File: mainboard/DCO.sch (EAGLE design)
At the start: 44 parts, among them IC101 LF353D, IC201 LF353D, IC3 V_REG_MIC2920, J3 M04X2, P101 TRIMPOT 100K

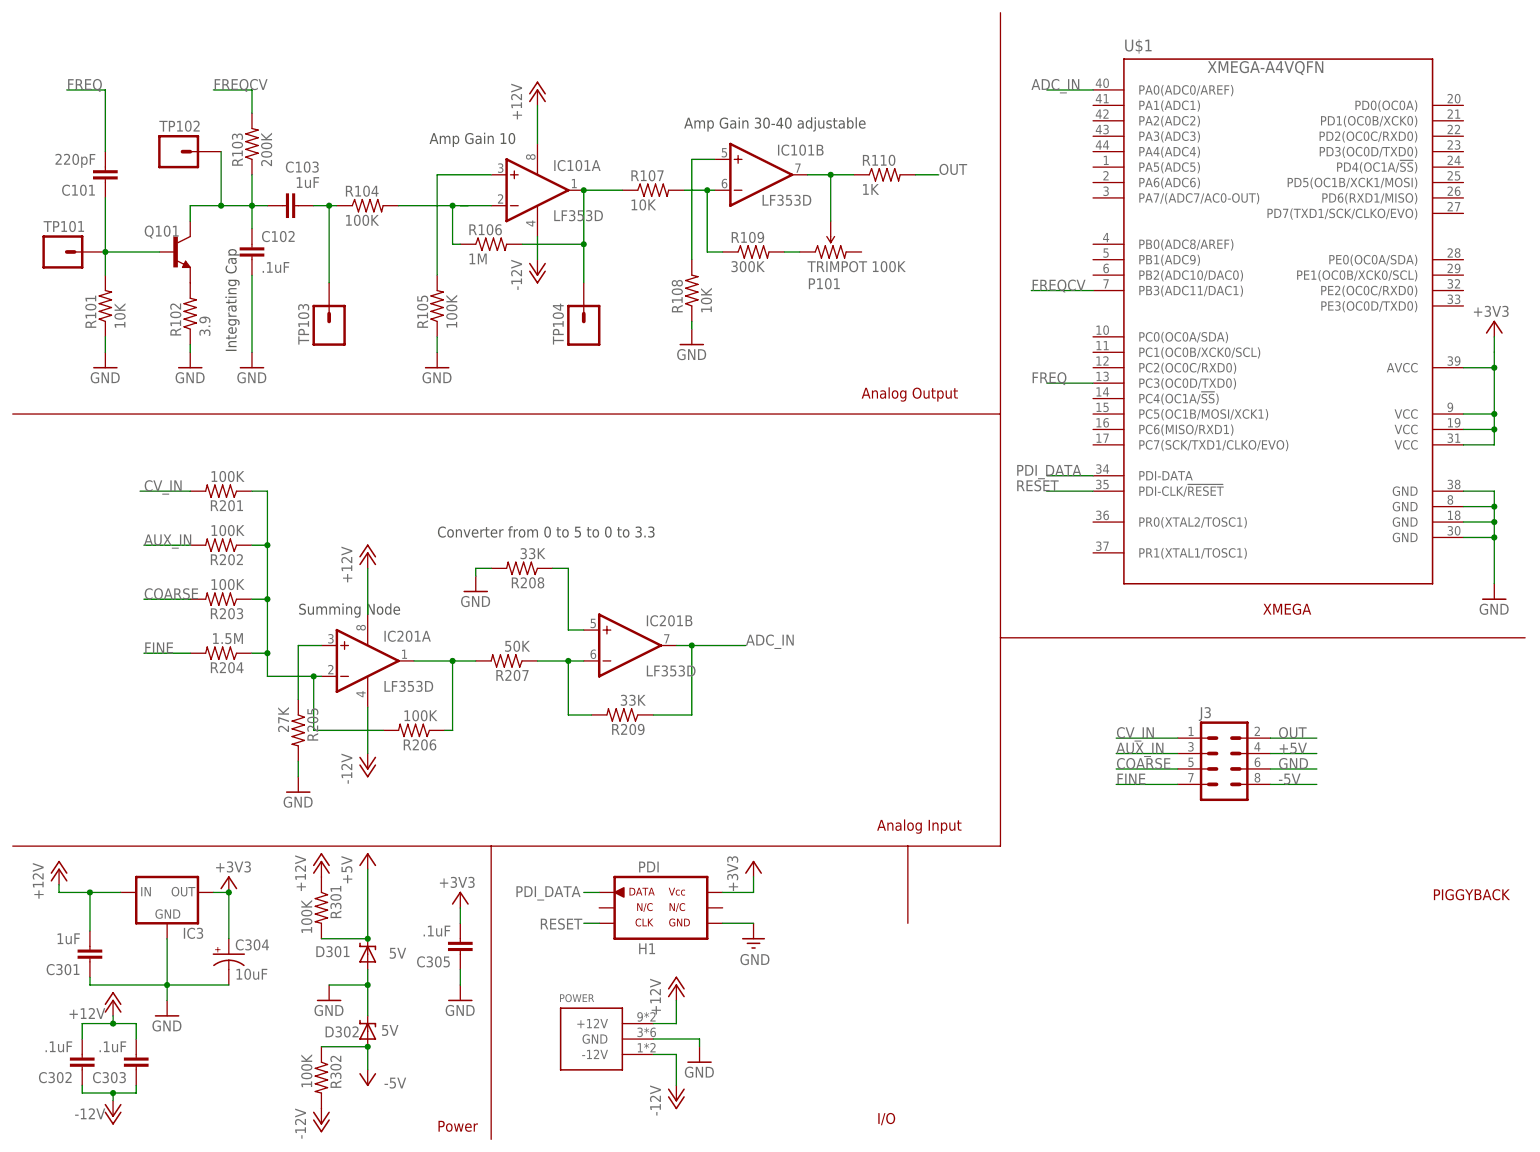
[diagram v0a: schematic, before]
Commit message: Re-laid out board, no routing
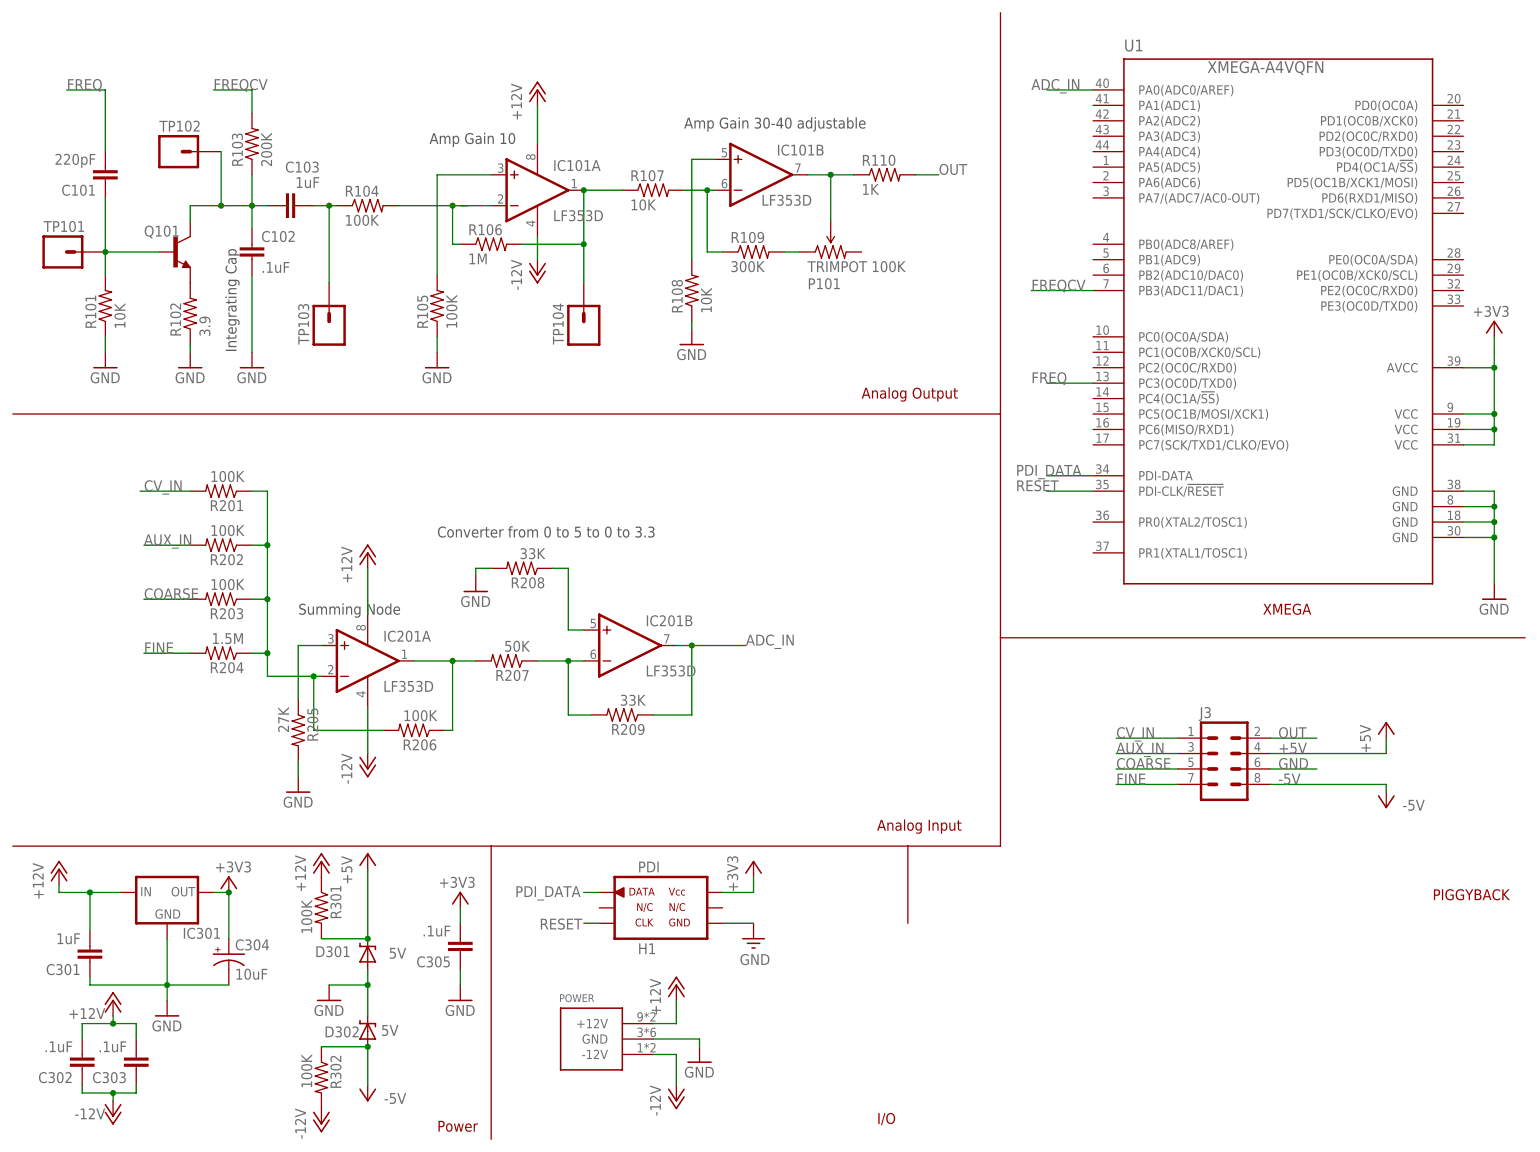
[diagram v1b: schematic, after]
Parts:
- renumbered IC3 to IC301, U$1 to U1
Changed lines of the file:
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@@
 <setting verticaltext="up"/>
 </settings>
-<grid distance="0.05" unitdist="inch" unit="inch" style="lines" multiple="1" display="no" altdistance="0.01" altunitdist="inch" altunit="inch"/>
+<grid distance="0.05" unitdist="inch" unit="inch" style="lines" multiple="1" display="yes" altdistance="0.01" altunitdist="inch" altunit="inch"/>
 <layers>
 <layer number="1" name="Top" color="4" fill="1" visible="no" active="no"/>
@@
 <part name="R207" library="SparkFun" deviceset="RESISTOR" device="0603-RES" value="50K"/>
 <part name="R209" library="SparkFun" deviceset="RESISTOR" device="0603-RES" value="33K"/>
-<part name="IC3" library="SparkFun" deviceset="V_REG_MIC2920" device="" value=""/>
+<part name="IC301" library="SparkFun" deviceset="V_REG_MIC2920" device="" value=""/>
 <part name="C301" library="SparkFun" deviceset="CAP" device="0603-CAP" value="1uF"/>
 <part name="C304" library="SparkFun" deviceset="CAP_POL" device="1206" value="10uF"/>
@@
 <part name="P+6" library="supply1" deviceset="+5V" device=""/>
 <part name="GND12" library="SparkFun" deviceset="GND" device=""/>
-<part name="U$1" library="custom" deviceset="XMEGA-A4" device="VQFN"/>
+<part name="U1" library="custom" deviceset="XMEGA-A4" device="VQFN"/>
 <part name="+3V2" library="supply1" deviceset="+3V3" device=""/>
 <part name="GND11" library="supply1" deviceset="GND" device=""/>
@@
 <part name="+3V4" library="supply1" deviceset="+3V3" device=""/>
 <part name="P+1" library="supply1" deviceset="+12V" device=""/>
+<part name="P+2" library="supply1" deviceset="+5V" device=""/>
+<part name="P-1" library="supply1" deviceset="-5V" device=""/>
 </parts>
 <sheets>
@@
 <instance part="R207" gate="G$1" x="81.28" y="78.74" rot="R180"/>
 <instance part="R209" gate="G$1" x="100.33" y="69.85" rot="R180"/>
-<instance part="IC3" gate="G$1" x="25.4" y="40.64"/>
+<instance part="IC301" gate="G$1" x="25.4" y="40.64"/>
 <instance part="C301" gate="G$1" x="12.7" y="31.75" rot="R180"/>
 <instance part="C304" gate="G$1" x="35.56" y="30.48"/>
@@
 <instance part="P+5" gate="1" x="50.8" y="45.72"/>
 <instance part="P-4" gate="1" x="50.8" y="2.54"/>
-<instance part="P-5" gate="1" x="58.42" y="8.89" smashed="yes">
-<attribute name="VALUE" x="64.77" y="10.16" size="1.778" layer="96" rot="R180"/>
+<instance part="P-5" gate="1" x="58.42" y="6.35" smashed="yes">
+<attribute name="VALUE" x="64.77" y="7.62" size="1.778" layer="96" rot="R180"/>
 </instance>
 <instance part="P+6" gate="1" x="58.42" y="46.99"/>
 <instance part="GND12" gate="1" x="243.84" y="88.9"/>
-<instance part="U$1" gate="G$1" x="208.28" y="137.16"/>
+<instance part="U1" gate="G$1" x="208.28" y="137.16"/>
 <instance part="+3V2" gate="G$1" x="73.66" y="40.64" smashed="yes">
 <attribute name="VALUE" x="76.2" y="43.18" size="1.778" layer="96" rot="R180"/>
@@
 </instance>
 <instance part="P+1" gate="1" x="86.36" y="172.72"/>
+<instance part="P+2" gate="1" x="226.06" y="68.58"/>
+<instance part="P-1" gate="1" x="226.06" y="54.61" smashed="yes">
+<attribute name="VALUE" x="232.41" y="55.88" size="1.778" layer="96" rot="R180"/>
+</instance>
 </instances>
 <busses>
@@
 </segment>
 <segment>
-<pinref part="U$1" gate="G$1" pin="PC3(OC0D/TXD0)"/>
+<pinref part="U1" gate="G$1" pin="PC3(OC0D/TXD0)"/>
 <wire x1="177.8" y1="124.46" x2="170.18" y2="124.46" width="0.1524" layer="91"/>
 <label x="167.64" y="124.46" size="1.778" layer="95"/>
@@
 </segment>
 <segment>
-<pinref part="U$1" gate="G$1" pin="PB3(ADC11/DAC1)"/>
+<pinref part="U1" gate="G$1" pin="PB3(ADC11/DAC1)"/>
 <wire x1="177.8" y1="139.7" x2="167.64" y2="139.7" width="0.1524" layer="91"/>
 <label x="167.64" y="139.7" size="1.778" layer="95"/>
@@
 </segment>
 <segment>
-<pinref part="IC3" gate="G$1" pin="GND"/>
+<pinref part="IC301" gate="G$1" pin="GND"/>
 <pinref part="GND9" gate="1" pin="GND"/>
 <wire x1="25.4" y1="33.02" x2="25.4" y2="25.4" width="0.1524" layer="91"/>
@@
 <junction x="243.84" y="99.06"/>
 <pinref part="GND12" gate="1" pin="GND"/>
-<pinref part="U$1" gate="G$1" pin="GND@1"/>
-<pinref part="U$1" gate="G$1" pin="GND@2"/>
-<pinref part="U$1" gate="G$1" pin="GND@3"/>
-<pinref part="U$1" gate="G$1" pin="GND@4"/>
+<pinref part="U1" gate="G$1" pin="GND@1"/>
+<pinref part="U1" gate="G$1" pin="GND@2"/>
+<pinref part="U1" gate="G$1" pin="GND@3"/>
+<pinref part="U1" gate="G$1" pin="GND@4"/>
 </segment>
 <segment>
@@
 <segment>
 <pinref part="J3" gate="G$1" pin="4"/>
-<wire x1="207.01" y1="63.5" x2="214.63" y2="63.5" width="0.1524" layer="91"/>
 <label x="208.28" y="63.5" size="1.778" layer="95"/>
+<wire x1="207.01" y1="63.5" x2="226.06" y2="63.5" width="0.1524" layer="91"/>
+<pinref part="P+2" gate="1" pin="+5V"/>
+<wire x1="226.06" y1="63.5" x2="226.06" y2="66.04" width="0.1524" layer="91"/>
 </segment>
 </net>
 <net name="-5V" class="0">
+<segment>
+<pinref part="J3" gate="G$1" pin="8"/>
+<label x="208.28" y="58.42" size="1.778" layer="95"/>
+<wire x1="207.01" y1="58.42" x2="226.06" y2="58.42" width="0.1524" layer="91"/>
+<pinref part="P-1" gate="1" pin="-5V"/>
+<wire x1="226.06" y1="58.42" x2="226.06" y2="57.15" width="0.1524" layer="91"/>
+</segment>
 <segment>
 <pinref part="D302" gate="G$1" pin="A"/>
@@
 <wire x1="58.42" y1="15.24" x2="50.8" y2="15.24" width="0.1524" layer="91"/>
 <pinref part="P-5" gate="1" pin="-5V"/>
-<wire x1="58.42" y1="15.24" x2="58.42" y2="11.43" width="0.1524" layer="91"/>
+<wire x1="58.42" y1="15.24" x2="58.42" y2="8.89" width="0.1524" layer="91"/>
 <junction x="58.42" y="15.24"/>
-</segment>
-<segment>
-<pinref part="J3" gate="G$1" pin="8"/>
-<wire x1="207.01" y1="58.42" x2="214.63" y2="58.42" width="0.1524" layer="91"/>
-<label x="208.28" y="58.42" size="1.778" layer="95"/>
 </segment>
 </net>
@@
 </segment>
 <segment>
-<pinref part="U$1" gate="G$1" pin="PA0(ADC0/AREF)"/>
+<pinref part="U1" gate="G$1" pin="PA0(ADC0/AREF)"/>
 <wire x1="177.8" y1="172.72" x2="170.18" y2="172.72" width="0.1524" layer="91"/>
 <label x="167.64" y="172.72" size="1.778" layer="95"/>
@@
 <pinref part="C301" gate="G$1" pin="2"/>
 <wire x1="12.7" y1="34.29" x2="12.7" y2="40.64" width="0.1524" layer="91"/>
-<pinref part="IC3" gate="G$1" pin="IN"/>
+<pinref part="IC301" gate="G$1" pin="IN"/>
 <wire x1="12.7" y1="40.64" x2="17.78" y2="40.64" width="0.1524" layer="91"/>
 <wire x1="12.7" y1="40.64" x2="7.62" y2="40.64" width="0.1524" layer="91"/>
@@
 <pinref part="C304" gate="G$1" pin="+"/>
 <wire x1="35.56" y1="33.02" x2="35.56" y2="40.64" width="0.1524" layer="91"/>
-<pinref part="IC3" gate="G$1" pin="OUT"/>
+<pinref part="IC301" gate="G$1" pin="OUT"/>
 <wire x1="35.56" y1="40.64" x2="33.02" y2="40.64" width="0.1524" layer="91"/>
 <pinref part="+3V1" gate="G$1" pin="+3V3"/>
@@
 <junction x="243.84" y="119.38"/>
 <junction x="243.84" y="116.84"/>
-<pinref part="U$1" gate="G$1" pin="AVCC"/>
-<pinref part="U$1" gate="G$1" pin="VCC@1"/>
-<pinref part="U$1" gate="G$1" pin="VCC@2"/>
-<pinref part="U$1" gate="G$1" pin="VCC@3"/>
+<pinref part="U1" gate="G$1" pin="AVCC"/>
+<pinref part="U1" gate="G$1" pin="VCC@1"/>
+<pinref part="U1" gate="G$1" pin="VCC@2"/>
+<pinref part="U1" gate="G$1" pin="VCC@3"/>
 <pinref part="+3V4" gate="G$1" pin="+3V3"/>
 </segment>
@@
 </segment>
 <segment>
-<pinref part="U$1" gate="G$1" pin="PDI-DATA"/>
+<pinref part="U1" gate="G$1" pin="PDI-DATA"/>
 <wire x1="177.8" y1="109.22" x2="170.18" y2="109.22" width="0.1524" layer="91"/>
 <label x="165.1" y="109.22" size="1.778" layer="95"/>
@@
 </segment>
 <segment>
-<pinref part="U$1" gate="G$1" pin="PDI-CLK/!RESET"/>
+<pinref part="U1" gate="G$1" pin="PDI-CLK/!RESET"/>
 <wire x1="177.8" y1="106.68" x2="170.18" y2="106.68" width="0.1524" layer="91"/>
 <label x="165.1" y="106.68" size="1.778" layer="95"/>

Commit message: edited schematic parts after sourcing from mouser, initial board layout.
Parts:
- C102: device SparkFun:CAP0805 -> SparkFun:CAP1210
- C301: device SparkFun:CAP0603-CAP -> SparkFun:CAP0805
- C304: device SparkFun:CAP_POL1206 -> SparkFun:CAP1206
- P101: device SparkFun:TRIMPOT -> SparkFun:TRIMPOTPTH
- R207: value 50K -> 51K
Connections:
- net +3V3: now also C304.1; no longer C304.+
- net GND: now also C304.2; no longer C304.-
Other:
- note added: "Converter from 0 to 5.1 to 0 to 3.3"
- note removed: "Converter from 0 to 5 to 0 to 3.3"
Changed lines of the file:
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@@
 <setting verticaltext="up"/>
 </settings>
-<grid distance="0.05" unitdist="inch" unit="inch" style="lines" multiple="1" display="yes" altdistance="0.01" altunitdist="inch" altunit="inch"/>
+<grid distance="0.05" unitdist="inch" unit="inch" style="lines" multiple="1" display="no" altdistance="0.01" altunitdist="inch" altunit="inch"/>
 <layers>
 <layer number="1" name="Top" color="4" fill="1" visible="no" active="no"/>
@@
 </classes>
 <parts>
-<part name="C102" library="SparkFun" deviceset="CAP" device="0805" value=".1uF"/>
+<part name="C102" library="SparkFun" deviceset="CAP" device="1210" value=".1uF"/>
 <part name="R103" library="SparkFun" deviceset="RESISTOR" device="0603-RES" value="200K"/>
 <part name="FRAME1" library="SparkFun" deviceset="FRAME-LETTER" device=""/>
@@
 <part name="R109" library="SparkFun" deviceset="RESISTOR" device="0603-RES" value="300K"/>
 <part name="R110" library="SparkFun" deviceset="RESISTOR" device="0603-RES" value="1K"/>
-<part name="P101" library="SparkFun" deviceset="TRIMPOT" device="" value="TRIMPOT 100K"/>
+<part name="P101" library="SparkFun" deviceset="TRIMPOT" device="PTH" value="TRIMPOT 100K"/>
 <part name="TP101" library="SparkFun" deviceset="M01" device="PTH" value=""/>
 <part name="TP102" library="SparkFun" deviceset="M01" device="PTH" value=""/>
@@
 <part name="GND8" library="supply1" deviceset="GND" device=""/>
 <part name="R208" library="SparkFun" deviceset="RESISTOR" device="0603-RES" value="33K"/>
-<part name="R207" library="SparkFun" deviceset="RESISTOR" device="0603-RES" value="50K"/>
+<part name="R207" library="SparkFun" deviceset="RESISTOR" device="0603-RES" value="51K"/>
 <part name="R209" library="SparkFun" deviceset="RESISTOR" device="0603-RES" value="33K"/>
 <part name="IC301" library="SparkFun" deviceset="V_REG_MIC2920" device="" value=""/>
-<part name="C301" library="SparkFun" deviceset="CAP" device="0603-CAP" value="1uF"/>
-<part name="C304" library="SparkFun" deviceset="CAP_POL" device="1206" value="10uF"/>
+<part name="C301" library="SparkFun" deviceset="CAP" device="0805" value="1uF"/>
 <part name="GND9" library="supply1" deviceset="GND" device=""/>
 <part name="P+3" library="supply1" deviceset="+12V" device=""/>
@@
 <part name="P+2" library="supply1" deviceset="+5V" device=""/>
 <part name="P-1" library="supply1" deviceset="-5V" device=""/>
+<part name="C304" library="SparkFun" deviceset="CAP" device="1206" value="10uF"/>
 </parts>
 <sheets>
@@
 <text x="110.49" y="166.37" size="1.778" layer="97">Amp Gain 30-40 adjustable</text>
 <text x="46.99" y="86.36" size="1.778" layer="97">Summing Node</text>
-<text x="69.85" y="99.06" size="1.778" layer="97">Converter from 0 to 5 to 0 to 3.3</text>
+<text x="69.85" y="99.06" size="1.778" layer="97">Converter from 0 to 5.1 to 0 to 3.3</text>
 <wire x1="0" y1="119.38" x2="162.56" y2="119.38" width="0.2032" layer="94"/>
 <wire x1="162.56" y1="119.38" x2="162.56" y2="185.42" width="0.2032" layer="94"/>
@@
 <instance part="IC301" gate="G$1" x="25.4" y="40.64"/>
 <instance part="C301" gate="G$1" x="12.7" y="31.75" rot="R180"/>
-<instance part="C304" gate="G$1" x="35.56" y="30.48"/>
 <instance part="GND9" gate="1" x="25.4" y="20.32"/>
 <instance part="P+3" gate="1" x="7.62" y="44.45"/>
@@
 <attribute name="VALUE" x="232.41" y="55.88" size="1.778" layer="96" rot="R180"/>
 </instance>
+<instance part="C304" gate="G$1" x="35.56" y="29.21"/>
 </instances>
 <busses>
@@
 <pinref part="GND9" gate="1" pin="GND"/>
 <wire x1="25.4" y1="33.02" x2="25.4" y2="25.4" width="0.1524" layer="91"/>
-<pinref part="C304" gate="G$1" pin="-"/>
 <wire x1="25.4" y1="25.4" x2="25.4" y2="22.86" width="0.1524" layer="91"/>
-<wire x1="35.56" y1="25.4" x2="25.4" y2="25.4" width="0.1524" layer="91"/>
 <junction x="25.4" y="25.4"/>
 <pinref part="C301" gate="G$1" pin="1"/>
 <wire x1="12.7" y1="26.67" x2="12.7" y2="25.4" width="0.1524" layer="91"/>
 <wire x1="12.7" y1="25.4" x2="25.4" y2="25.4" width="0.1524" layer="91"/>
+<wire x1="25.4" y1="25.4" x2="35.56" y2="25.4" width="0.1524" layer="91"/>
+<pinref part="C304" gate="G$1" pin="2"/>
+<wire x1="35.56" y1="25.4" x2="35.56" y2="26.67" width="0.1524" layer="91"/>
 </segment>
 <segment>
@@
 <net name="+3V3" class="0">
 <segment>
-<pinref part="C304" gate="G$1" pin="+"/>
-<wire x1="35.56" y1="33.02" x2="35.56" y2="40.64" width="0.1524" layer="91"/>
+<wire x1="35.56" y1="34.29" x2="35.56" y2="40.64" width="0.1524" layer="91"/>
 <pinref part="IC301" gate="G$1" pin="OUT"/>
 <wire x1="35.56" y1="40.64" x2="33.02" y2="40.64" width="0.1524" layer="91"/>
 <pinref part="+3V1" gate="G$1" pin="+3V3"/>
 <junction x="35.56" y="40.64"/>
-</segment>
-<segment>
+<pinref part="C304" gate="G$1" pin="1"/>
+</segment>
+<segment>

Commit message: brendan said it was a good idea to add a ground via near the decoupling cap for the micro
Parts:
- P101: device SparkFun:TRIMPOTPTH -> SparkFun:TRIMPOT
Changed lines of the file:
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@@
 <part name="R109" library="SparkFun" deviceset="RESISTOR" device="0603-RES" value="300K"/>
 <part name="R110" library="SparkFun" deviceset="RESISTOR" device="0603-RES" value="1K"/>
-<part name="P101" library="SparkFun" deviceset="TRIMPOT" device="PTH" value="TRIMPOT 100K"/>
+<part name="P101" library="SparkFun" deviceset="TRIMPOT" device="" value="TRIMPOT 100K"/>
 <part name="TP101" library="SparkFun" deviceset="M01" device="PTH" value=""/>
 <part name="TP102" library="SparkFun" deviceset="M01" device="PTH" value=""/>

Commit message: Another attempt to layout DCO.
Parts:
- P101: device SparkFun:TRIMPOT -> SparkFun:TRIMPOTPTH
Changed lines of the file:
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@@
 <setting verticaltext="up"/>
 </settings>
-<grid distance="0.05" unitdist="inch" unit="inch" style="lines" multiple="1" display="no" altdistance="0.01" altunitdist="inch" altunit="inch"/>
+<grid distance="0.1" unitdist="inch" unit="inch" style="lines" multiple="1" display="no" altdistance="0.01" altunitdist="inch" altunit="inch"/>
 <layers>
 <layer number="1" name="Top" color="4" fill="1" visible="no" active="no"/>
@@
 <part name="R109" library="SparkFun" deviceset="RESISTOR" device="0603-RES" value="300K"/>
 <part name="R110" library="SparkFun" deviceset="RESISTOR" device="0603-RES" value="1K"/>
-<part name="P101" library="SparkFun" deviceset="TRIMPOT" device="" value="TRIMPOT 100K"/>
+<part name="P101" library="SparkFun" deviceset="TRIMPOT" device="PTH" value="TRIMPOT 100K"/>
 <part name="TP101" library="SparkFun" deviceset="M01" device="PTH" value=""/>
 <part name="TP102" library="SparkFun" deviceset="M01" device="PTH" value=""/>
